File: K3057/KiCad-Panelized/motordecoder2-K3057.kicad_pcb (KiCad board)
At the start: 2 copper layers, 85 x 94 mm, 522 parts, among them J11 PAD, J12 PAD, J14 PAD, J16 PAD, J18 PAD, J19 PAD, P10 PAD, P11 PAD, P21 PAD, P22 PAD, P23 PAD, P24 PAD, P25 PAD, P26 PAD, P27 PAD, P28 PAD, P29 PAD, P31 PAD, P7 PAD, P8 PAD, P9 PROG, Q1 DMG6601LVT, Q11 SSM6N7002BFE, Q12 SSM6N7002BFE, Q13 SSM6N7002BFE, Q14 SSM6N7002BFE, Q15 SSM3K7002BFU, Q2 DMG6601LVT, Q21 PMBT3906VS, Q22 SSM6N7002BFE, Q3 PMBT3904VS, Q5 2SC4116, Q6 PMBT3906VS, Q8 PMBT3904VS, U2 ATtiny1606-M

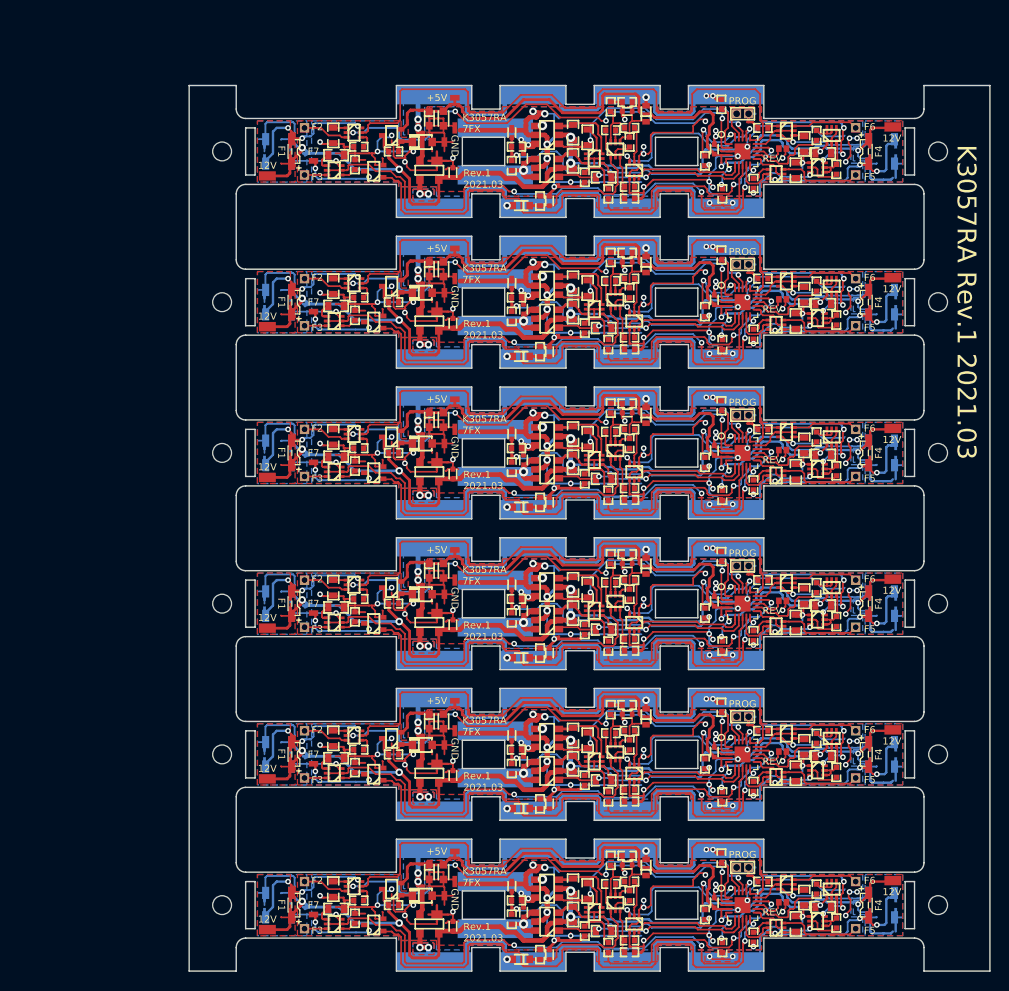
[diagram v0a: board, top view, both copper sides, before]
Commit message: 回路の問題点を修正 (K3066: Rev3 / それ以外: Rev2)
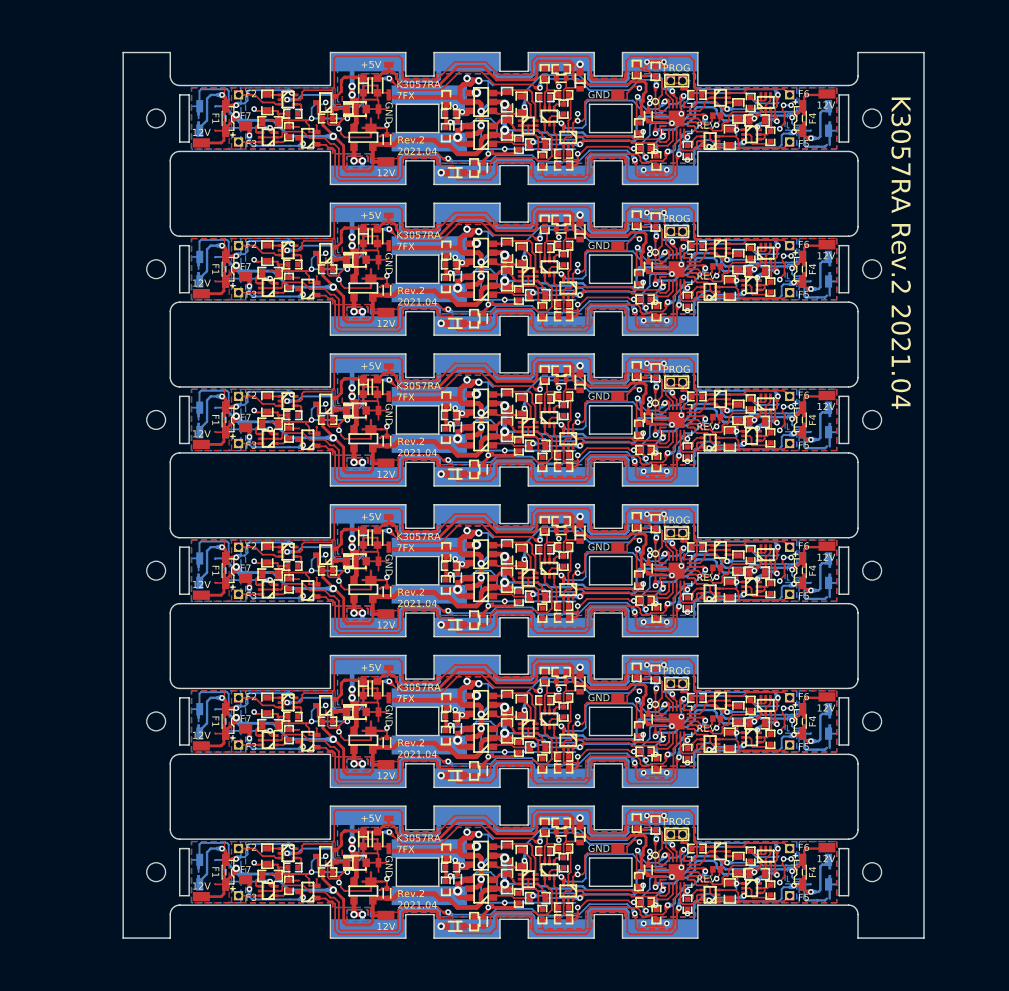
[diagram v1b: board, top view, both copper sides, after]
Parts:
- removed the C1 at (136.0, 126.2)
- removed the C1 at (136.0, 110.2)
- removed the C1 at (136.0, 94.2)
- removed the C1 at (136.0, 78.2)
- removed the C1 at (136.0, 62.2)
- removed the C11 at (154.5, 119.8)
- removed the C11 at (154.5, 103.8)
- removed the C11 at (154.5, 87.8)
- removed the C11 at (154.5, 71.8)
- removed the C11 at (154.5, 55.8)
- removed the C12 at (146.2, 129.2)
- removed the C12 at (146.2, 113.2)
- removed the C12 at (146.2, 97.2)
- removed the C12 at (146.2, 81.2)
- removed the C12 at (146.2, 65.2)
- removed the C3 at (135.0, 120.5)
- removed the C3 at (135.0, 104.5)
- removed the C3 at (135.0, 88.5)
- removed the C3 at (135.0, 72.5)
- removed the C3 at (135.0, 56.5)
- removed the C4 at (133.5, 120.5)
- removed the C4 at (133.5, 104.5)
- removed the C4 at (133.5, 88.5)
- removed the C4 at (133.5, 72.5)
- removed the C4 at (133.5, 56.5)
- removed the C5 at (163.8, 123.8)
- removed the C5 at (163.8, 107.8)
- removed the C5 at (163.8, 91.8)
- removed the C5 at (163.8, 75.8)
- removed the C5 at (163.8, 59.8)
- removed C6 (x6): 104, footprint:C_1005_v2
- removed the C7 at (143.5, 124.8)
- removed the C7 at (143.5, 108.8)
- removed the C7 at (143.5, 92.8)
- removed the C7 at (143.5, 76.8)
- removed the C7 at (143.5, 60.8)
- removed the D1 at (133.5, 126.0)
- removed the D1 at (133.5, 110.0)
- removed the D1 at (133.5, 94.0)
- removed the D1 at (133.5, 78.0)
- removed the D1 at (133.5, 62.0)
- removed the D11 at (118.5, 124.0)
- removed the D11 at (118.5, 108.0)
- removed the D11 at (118.5, 92.0)
- removed the D11 at (118.5, 76.0)
- removed the D11 at (118.5, 60.0)
- removed the D12 at (180.5, 124.0)
- removed the D12 at (180.5, 108.0)
- removed the D12 at (180.5, 92.0)
- removed the D12 at (180.5, 76.0)
- removed the D12 at (180.5, 60.0)
- removed the D13 at (115.8, 124.0)
- removed the D13 at (115.8, 108.0)
- removed the D13 at (115.8, 92.0)
- removed the D13 at (115.8, 76.0)
- removed the D13 at (115.8, 60.0)
- removed the D14 at (183.2, 124.0)
- removed the D14 at (183.2, 108.0)
- removed the D14 at (183.2, 92.0)
- removed the D14 at (183.2, 76.0)
- removed the D14 at (183.2, 60.0)
- removed the D15 at (180.5, 124.0)
- removed the D15 at (180.5, 108.0)
- removed the D15 at (180.5, 92.0)
- removed the D15 at (180.5, 76.0)
- removed the D15 at (180.5, 60.0)
- removed the D16 at (118.5, 124.0)
- removed the D16 at (118.5, 108.0)
- removed the D16 at (118.5, 92.0)
- removed the D16 at (118.5, 76.0)
- removed the D16 at (118.5, 60.0)
- removed the D21 at (156.5, 120.0)
- removed the D21 at (156.5, 104.0)
- removed the D21 at (156.5, 88.0)
- removed the D21 at (156.5, 72.0)
- removed the D21 at (156.5, 56.0)
- removed the D22 at (143.2, 129.8)
- removed the D22 at (143.2, 113.8)
- removed the D22 at (143.2, 97.8)
- removed the D22 at (143.2, 81.8)
- removed the D22 at (143.2, 65.8)
- removed the D3 at (132.8, 123.0)
- removed the D3 at (132.8, 107.0)
- removed the D3 at (132.8, 91.0)
- removed the D3 at (132.8, 75.0)
- removed the D3 at (132.8, 59.0)
- removed the J11 at (182.7, 121.4)
- removed the J11 at (182.7, 105.4)
- removed the J11 at (182.7, 89.4)
- removed the J11 at (182.7, 73.4)
- removed the J11 at (182.7, 57.4)
- removed the J12 at (178.8, 126.5)
- removed the J12 at (178.8, 110.5)
- removed the J12 at (178.8, 94.5)
- removed the J12 at (178.8, 78.5)
- removed the J12 at (178.8, 62.5)
- removed the J14 at (120.2, 126.5)
- removed the J14 at (120.2, 110.5)
- removed the J14 at (120.2, 94.5)
- removed the J14 at (120.2, 78.5)
- removed the J14 at (120.2, 62.5)
- removed the J16 at (178.8, 121.5)
- removed the J16 at (178.8, 105.5)
- removed the J16 at (178.8, 89.5)
- removed the J16 at (178.8, 73.5)
- removed the J16 at (178.8, 57.5)
- removed the J18 at (120.2, 121.5)
- removed the J18 at (120.2, 105.5)
- removed the J18 at (120.2, 89.5)
- removed the J18 at (120.2, 73.5)
- removed the J18 at (120.2, 57.5)
- removed the J19 at (121.2, 125.0)
- removed the J19 at (121.2, 109.0)
- removed the J19 at (121.2, 93.0)
- removed the J19 at (121.2, 77.0)
- removed the J19 at (121.2, 61.0)
- removed the J19 at (121.2, 45.0)
- removed the JP1 at (171.0, 123.7)
- removed the JP1 at (171.0, 107.7)
- removed the JP1 at (171.0, 91.7)
- removed the JP1 at (171.0, 75.7)
- removed the JP1 at (171.0, 59.7)
- removed the P10 at (136.2, 118.3)
- removed the P10 at (136.2, 102.3)
- removed the P10 at (136.2, 86.3)
- removed the P10 at (136.2, 70.3)
- removed the P10 at (136.2, 54.3)
- removed the P11 at (136.2, 121.5)
- removed the P11 at (136.2, 105.5)
- removed the P11 at (136.2, 89.5)
- removed the P11 at (136.2, 73.5)
- removed the P11 at (136.2, 57.5)
- removed the P21 at (134.0, 118.0)
- removed the P21 at (134.0, 102.0)
- removed the P21 at (134.0, 86.0)
- removed the P21 at (134.0, 70.0)
- removed the P21 at (134.0, 54.0)
- removed the P22 at (144.5, 118.0)
- removed the P22 at (144.5, 102.0)
- removed the P22 at (144.5, 86.0)
- removed the P22 at (144.5, 70.0)
- removed the P22 at (144.5, 54.0)
- removed the P23 at (154.5, 118.0)
- removed the P23 at (154.5, 102.0)
- removed the P23 at (154.5, 86.0)
- removed the P23 at (154.5, 70.0)
- removed the P23 at (154.5, 54.0)
- removed the P24 at (165.0, 118.0)
- removed the P24 at (165.0, 102.0)
- removed the P24 at (165.0, 86.0)
- removed the P24 at (165.0, 70.0)
- removed the P24 at (165.0, 54.0)
- removed the P25 at (134.0, 130.0)
- removed the P25 at (134.0, 114.0)
- removed the P25 at (134.0, 98.0)
- removed the P25 at (134.0, 82.0)
- removed the P25 at (134.0, 66.0)
- removed the P26 at (144.5, 130.0)
- removed the P26 at (144.5, 114.0)
- removed the P26 at (144.5, 98.0)
- removed the P26 at (144.5, 82.0)
- removed the P26 at (144.5, 66.0)
- removed the P27 at (154.5, 130.0)
- removed the P27 at (154.5, 114.0)
- removed the P27 at (154.5, 98.0)
- removed the P27 at (154.5, 82.0)
- removed the P27 at (154.5, 66.0)
- removed the P28 at (165.0, 130.0)
- removed the P28 at (165.0, 114.0)
- removed the P28 at (165.0, 98.0)
- removed the P28 at (165.0, 82.0)
- removed the P28 at (165.0, 66.0)
- removed the P29 at (140.5, 121.5)
- removed the P29 at (140.5, 105.5)
- removed the P29 at (140.5, 89.5)
- removed the P29 at (140.5, 73.5)
- removed the P29 at (140.5, 57.5)
- removed the P31 at (140.5, 126.5)
- removed the P31 at (140.5, 110.5)
- removed the P31 at (140.5, 94.5)
- removed the P31 at (140.5, 78.5)
- removed the P31 at (140.5, 62.5)
- removed the P7 at (116.3, 126.6)
- removed the P7 at (116.3, 110.6)
- removed the P7 at (116.3, 94.6)
- removed the P7 at (116.3, 78.6)
- removed the P7 at (116.3, 62.6)
- removed the P8 at (135.1, 123.0)
- removed the P8 at (135.1, 107.0)
- removed the P8 at (135.1, 91.0)
- removed the P8 at (135.1, 75.0)
- removed the P8 at (135.1, 59.0)
- removed the P9 at (166.8, 120.0)
- removed the P9 at (166.8, 104.0)
- removed the P9 at (166.8, 88.0)
- removed the P9 at (166.8, 72.0)
- removed the P9 at (166.8, 56.0)
- removed the Q1 at (146.0, 122.2)
- removed the Q1 at (146.0, 106.2)
- removed the Q1 at (146.0, 90.2)
- removed the Q1 at (146.0, 74.2)
- removed the Q1 at (146.0, 58.2)
- removed the Q11 at (125.5, 122.0)
- removed the Q11 at (125.5, 106.0)
- removed the Q11 at (125.5, 90.0)
- removed the Q11 at (125.5, 74.0)
- removed the Q11 at (125.5, 58.0)
- removed the Q12 at (170.3, 126.4)
- removed the Q12 at (170.3, 110.4)
- removed the Q12 at (170.3, 94.4)
- removed the Q12 at (170.3, 78.4)
- removed the Q12 at (170.3, 62.4)
- removed the Q13 at (123.4, 126.0)
- removed the Q13 at (123.4, 110.0)
- removed the Q13 at (123.4, 94.0)
- removed the Q13 at (123.4, 78.0)
- removed the Q13 at (123.4, 62.0)
- removed the Q14 at (171.4, 121.8)
- removed the Q14 at (171.4, 105.8)
- removed the Q14 at (171.4, 89.8)
- removed the Q14 at (171.4, 73.8)
- removed the Q14 at (171.4, 57.8)
- removed the Q15 at (127.6, 126.1)
- removed the Q15 at (127.6, 110.1)
- removed the Q15 at (127.6, 94.1)
- removed the Q15 at (127.6, 78.1)
- removed the Q15 at (127.6, 62.1)
- removed the Q2 at (146.0, 125.8)
- removed the Q2 at (146.0, 109.8)
- removed the Q2 at (146.0, 93.8)
- removed the Q2 at (146.0, 77.8)
- removed the Q2 at (146.0, 61.8)
- removed the Q21 at (153.2, 123.8)
- removed the Q21 at (153.2, 107.8)
- removed the Q21 at (153.2, 91.8)
- removed the Q21 at (153.2, 75.8)
- removed the Q21 at (153.2, 59.8)
- removed the Q22 at (155.2, 126.0)
- removed the Q22 at (155.2, 110.0)
- removed the Q22 at (155.2, 94.0)
- removed the Q22 at (155.2, 78.0)
- removed the Q22 at (155.2, 62.0)
- removed the Q3 at (151.0, 124.8)
- removed the Q3 at (151.0, 108.8)
- removed the Q3 at (151.0, 92.8)
- removed the Q3 at (151.0, 76.8)
- removed the Q3 at (151.0, 60.8)
- removed the Q5 at (129.5, 122.3)
- removed the Q5 at (129.5, 106.3)
- removed the Q5 at (129.5, 90.3)
- removed the Q5 at (129.5, 74.3)
- removed the Q5 at (129.5, 58.3)
- removed the Q6 at (176.2, 122.3)
- removed the Q6 at (176.2, 106.3)
- removed the Q6 at (176.2, 90.3)
- removed the Q6 at (176.2, 74.3)
- removed the Q6 at (176.2, 58.3)
- removed the Q8 at (174.7, 125.7)
- removed the Q8 at (174.7, 109.7)
- removed the Q8 at (174.7, 93.7)
- removed the Q8 at (174.7, 77.7)
- removed the Q8 at (174.7, 61.7)
- removed the R1 at (164.5, 119.0)
- removed the R1 at (164.5, 103.0)
- removed the R1 at (164.5, 87.0)
- removed the R1 at (164.5, 71.0)
- removed the R1 at (164.5, 55.0)
- removed the R10 at (142.2, 125.5)
- removed the R10 at (142.2, 109.5)
- removed the R10 at (142.2, 93.5)
- removed the R10 at (142.2, 77.5)
- removed the R10 at (142.2, 61.5)
- removed the R11 at (162.8, 125.0)
- removed the R11 at (162.8, 109.0)
- removed the R11 at (162.8, 93.0)
- removed the R11 at (162.8, 77.0)
- removed the R11 at (162.8, 61.0)
- removed the R12 at (129.7, 124.0)
- removed the R12 at (129.7, 108.0)
- removed the R12 at (129.7, 92.0)
- removed the R12 at (129.7, 76.0)
- removed the R12 at (129.7, 60.0)
- removed the R13 at (174.6, 122.3)
- removed the R13 at (174.6, 106.3)
- removed the R13 at (174.6, 90.3)
- removed the R13 at (174.6, 74.3)
- removed the R13 at (174.6, 58.3)
- removed the R14 at (175.3, 124.2)
- removed the R14 at (175.3, 108.2)
- removed the R14 at (175.3, 92.2)
- removed the R14 at (175.3, 76.2)
- removed the R14 at (175.3, 60.2)
- removed the R15 at (176.7, 125.9)
- removed the R15 at (176.7, 109.9)
- removed the R15 at (176.7, 93.9)
- removed the R15 at (176.7, 77.9)
- removed the R15 at (176.7, 61.9)
- removed the R2 at (164.6, 128.5)
- removed the R2 at (164.6, 112.5)
- removed the R2 at (164.6, 96.5)
- removed the R2 at (164.6, 80.5)
- removed the R2 at (164.6, 64.5)
- removed the R21 at (123.3, 122.3)
- removed the R21 at (123.3, 106.3)
- removed the R21 at (123.3, 90.3)
- removed the R21 at (123.3, 74.3)
- removed the R21 at (123.3, 58.3)
- removed the R22 at (172.4, 126.0)
- removed the R22 at (172.4, 110.0)
- removed the R22 at (172.4, 94.0)
- removed the R22 at (172.4, 78.0)
- removed the R22 at (172.4, 62.0)
- removed the R23 at (167.9, 127.4)
- removed the R23 at (167.9, 111.4)
- removed the R23 at (167.9, 95.4)
- removed the R23 at (167.9, 79.4)
- removed the R23 at (167.9, 63.4)
- removed the R24 at (125.6, 125.4)
- removed the R24 at (125.6, 109.4)
- removed the R24 at (125.6, 93.4)
- removed the R24 at (125.6, 77.4)
- removed the R24 at (125.6, 61.4)
- removed the R25 at (168.9, 121.5)
- removed the R25 at (168.9, 105.5)
- removed the R25 at (168.9, 89.5)
- removed the R25 at (168.9, 73.5)
- removed the R25 at (168.9, 57.5)
- removed the R26 at (126.0, 123.5)
- removed the R26 at (126.0, 107.5)
- removed the R26 at (126.0, 91.5)
- removed the R26 at (126.0, 75.5)
- removed the R26 at (126.0, 59.5)
- removed the R27 at (123.6, 124.4)
- removed the R27 at (123.6, 108.4)
- removed the R27 at (123.6, 92.4)
- removed the R27 at (123.6, 76.4)
- removed the R27 at (123.6, 60.4)
- removed the R28 at (173.3, 123.2)
- removed the R28 at (173.3, 107.2)
- removed the R28 at (173.3, 91.2)
- removed the R28 at (173.3, 75.2)
- removed the R28 at (173.3, 59.2)
- removed the R3 at (148.8, 122.0)
- removed the R3 at (148.8, 106.0)
- removed the R3 at (148.8, 90.0)
- removed the R3 at (148.8, 74.0)
- removed the R3 at (148.8, 58.0)
- removed the R31 at (154.8, 123.0)
- removed the R31 at (154.8, 107.0)
- removed the R31 at (154.8, 91.0)
- removed the R31 at (154.8, 75.0)
- removed the R31 at (154.8, 59.0)
- removed the R32 at (154.5, 118.8)
- removed the R32 at (154.5, 102.8)
- removed the R32 at (154.5, 86.8)
- removed the R32 at (154.5, 70.8)
- removed the R32 at (154.5, 54.8)
- removed the R33 at (152.8, 119.2)
- removed the R33 at (152.8, 103.2)
- removed the R33 at (152.8, 87.2)
- removed the R33 at (152.8, 71.2)
- removed the R33 at (152.8, 55.2)
- removed the R34 at (154.8, 121.5)
- removed the R34 at (154.8, 105.5)
- removed the R34 at (154.8, 89.5)
- removed the R34 at (154.8, 73.5)
- removed the R34 at (154.8, 57.5)
- removed the R35 at (152.8, 121.8)
- removed the R35 at (152.8, 105.8)
- removed the R35 at (152.8, 89.8)
- removed the R35 at (152.8, 73.8)
- removed the R35 at (152.8, 57.8)
- removed the R36 at (145.2, 129.2)
- removed the R36 at (145.2, 113.2)
- removed the R36 at (145.2, 97.2)
- removed the R36 at (145.2, 81.2)
- removed the R36 at (145.2, 65.2)
- removed the R37 at (154.8, 129.0)
- removed the R37 at (154.8, 113.0)
- removed the R37 at (154.8, 97.0)
- removed the R37 at (154.8, 81.0)
- removed the R37 at (154.8, 65.0)
- removed the R38 at (154.8, 127.8)
- removed the R38 at (154.8, 111.8)
- removed the R38 at (154.8, 95.8)
- removed the R38 at (154.8, 79.8)
- removed the R38 at (154.8, 63.8)
- removed the R4 at (148.8, 125.0)
- removed the R4 at (148.8, 109.0)
- removed the R4 at (148.8, 93.0)
- removed the R4 at (148.8, 77.0)
- removed the R4 at (148.8, 61.0)
- removed the R5 at (150.3, 122.5)
- removed the R5 at (150.3, 106.5)
- removed the R5 at (150.3, 90.5)
- removed the R5 at (150.3, 74.5)
- removed the R5 at (150.3, 58.5)
- removed the R6 at (152.0, 126.8)
- removed the R6 at (152.0, 110.8)
- removed the R6 at (152.0, 94.8)
- removed the R6 at (152.0, 78.8)
- removed the R6 at (152.0, 62.8)
- removed the R7 at (152.5, 128.5)
- removed the R7 at (152.5, 112.5)
- removed the R7 at (152.5, 96.5)
- removed the R7 at (152.5, 80.5)
- removed the R7 at (152.5, 64.5)
- removed the R8 at (150.0, 126.8)
- removed the R8 at (150.0, 110.8)
- removed the R8 at (150.0, 94.8)
- removed the R8 at (150.0, 78.8)
- removed the R8 at (150.0, 62.8)
- removed the R9 at (142.8, 123.5)
- removed the R9 at (142.8, 107.5)
- removed the R9 at (142.8, 91.5)
- removed the R9 at (142.8, 75.5)
- removed the R9 at (142.8, 59.5)
- removed the REF** at (187.5, 60.0)
- removed the REF** at (111.5, 60.0)
- removed the REF** at (187.5, 44.0)
- removed the REF** at (111.5, 44.0)
- removed the REF** at (187.5, 76.0)
- removed the REF** at (187.5, 92.0)
- removed the REF** at (187.5, 108.0)
- removed the REF** at (187.5, 124.0)
- removed the REF** at (111.5, 124.0)
- removed the REF** at (111.5, 108.0)
- removed the REF** at (111.5, 92.0)
- removed the REF** at (111.5, 76.0)
- removed the U2 at (166.8, 124.0)
- removed the U2 at (166.8, 108.0)
- removed the U2 at (166.8, 92.0)
- removed the U2 at (166.8, 76.0)
- removed the U2 at (166.8, 60.0)
- added C1: 104, footprint:C_1005_v2, F.Cu at (129.0, 122.8)
- added C1: 104, footprint:C_1005_v2, F.Cu at (129.0, 106.8)
- added C1: 104, footprint:C_1005_v2, F.Cu at (129.0, 90.8)
- added C1: 104, footprint:C_1005_v2, F.Cu at (129.0, 74.8)
- added C1: 104, footprint:C_1005_v2, F.Cu at (129.0, 58.8)
- added C11: 105, footprint:C_1005_v2, F.Cu at (147.5, 116.2)
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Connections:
- net Func8 renamed DIR_JP
- Q11 pad 5: Func6 -> Func2
- Q12 pad 2: Func2 -> Func4
- Q12 pad 5: Func3 -> Func5
- Q13 pad 2: Func4 -> Func3
- Q13 pad 5: Func4 -> Func3
- Q14 pad 2: Func5 -> Func6
- Q14 pad 5: Func5 -> Func6
- U2 pad 11: Func2 -> Func4
- U2 pad 15: Func5 -> Func6
- U2 pad 16: Func6 -> Func2
- U2 pad 8: Func4 -> Func3
- U2 pad 9: Func3 -> Func5
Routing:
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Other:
- rule pad_to_mask_clearance: 0 -> 0.05
- board text added: "K3057RA Rev.2 2021.04"
- board text added: "Rev.2 2021.04"
- board text removed: "K3057RA Rev.1 2021.03"
- board text removed: "Rev.1 2021.03"

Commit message: 基板上のF表記をP表記に変更
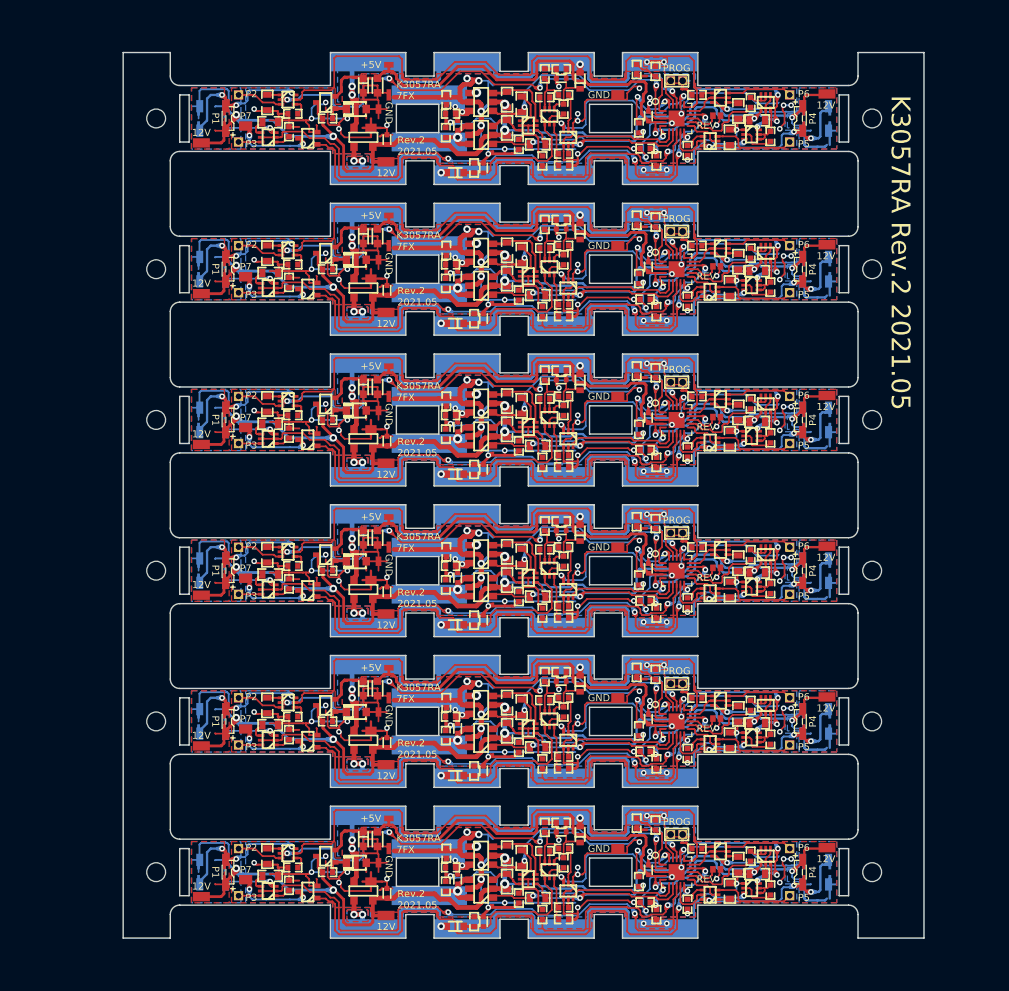
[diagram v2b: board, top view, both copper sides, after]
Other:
- board text added: "K3057RA Rev.2 2021.05"
- board text added: "P1"
- board text added: "P2"
- board text added: "P3"
- board text added: "P4"
- board text added: "P5"
- board text added: "P6"
- board text added: "P7"
- board text added: "Rev.2 2021.05"
- board text removed: "F1"
- board text removed: "F2"
- board text removed: "F3"
- board text removed: "F4"
- board text removed: "F5"
- board text removed: "F6"
- board text removed: "F7"
- board text removed: "K3057RA Rev.2 2021.04"
- board text removed: "Rev.2 2021.04"

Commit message: (K3057RA) 表面のLEDパッドを増設
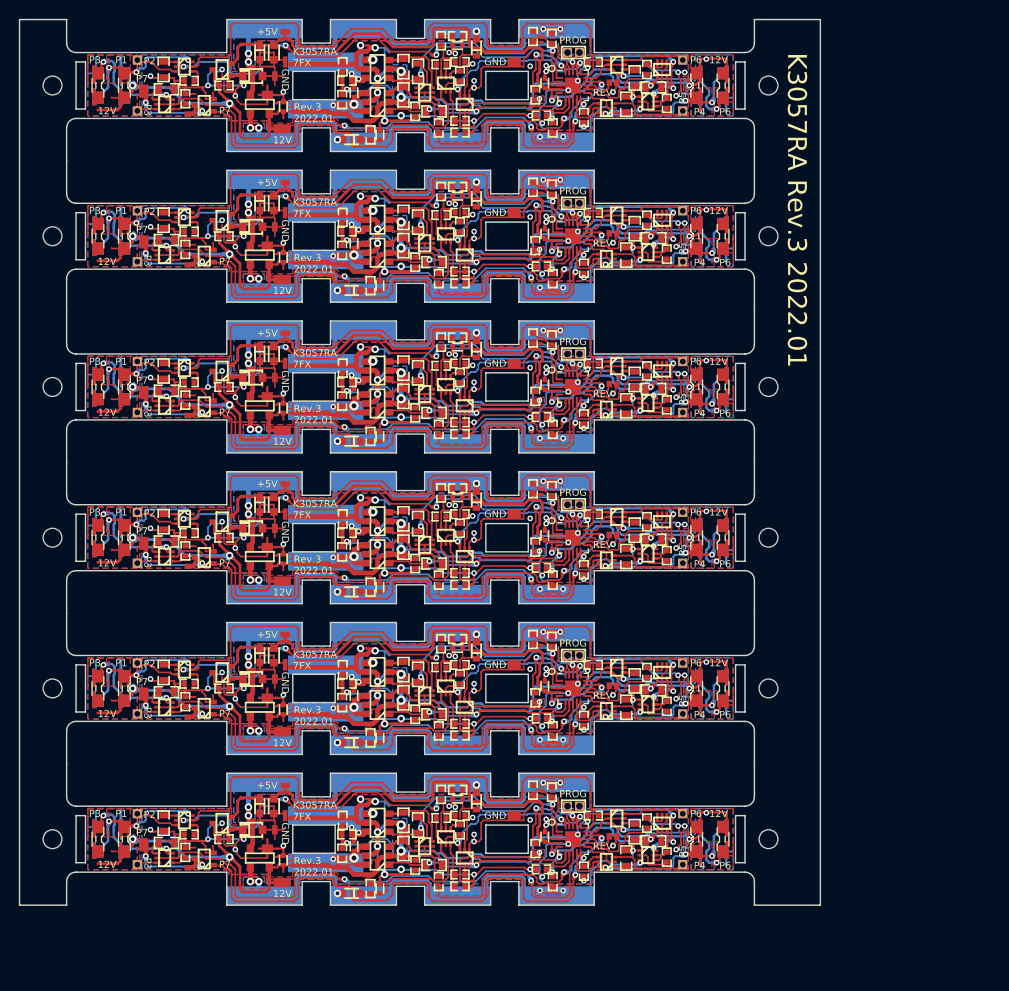
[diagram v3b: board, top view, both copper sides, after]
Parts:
- removed the C1 at (129.0, 122.8)
- removed the C1 at (129.0, 106.8)
- removed the C1 at (129.0, 90.8)
- removed the C1 at (129.0, 74.8)
- removed the C1 at (129.0, 58.8)
- removed the C11 at (147.5, 116.2)
- removed the C11 at (147.5, 100.2)
- removed the C11 at (147.5, 84.2)
- removed the C11 at (147.5, 68.2)
- removed the C11 at (147.5, 52.2)
- removed the C12 at (139.2, 125.8)
- removed the C12 at (139.2, 109.8)
- removed the C12 at (139.2, 93.8)
- removed the C12 at (139.2, 77.8)
- removed the C12 at (139.2, 61.8)
- removed the C3 at (128.0, 117.0)
- removed the C3 at (128.0, 101.0)
- removed the C3 at (128.0, 85.0)
- removed the C3 at (128.0, 69.0)
- removed the C3 at (128.0, 53.0)
- removed the C4 at (126.5, 117.0)
- removed the C4 at (126.5, 101.0)
- removed the C4 at (126.5, 85.0)
- removed the C4 at (126.5, 69.0)
- removed the C4 at (126.5, 53.0)
- removed the C5 at (156.8, 120.2)
- removed the C5 at (156.8, 104.2)
- removed the C5 at (156.8, 88.2)
- removed the C5 at (156.8, 72.2)
- removed the C5 at (156.8, 56.2)
- removed the C7 at (136.5, 121.2)
- removed the C7 at (136.5, 105.2)
- removed the C7 at (136.5, 89.2)
- removed the C7 at (136.5, 73.2)
- removed the C7 at (136.5, 57.2)
- removed the D1 at (126.5, 122.5)
- removed the D1 at (126.5, 106.5)
- removed the D1 at (126.5, 90.5)
- removed the D1 at (126.5, 74.5)
- removed the D1 at (126.5, 58.5)
- removed the D11 at (111.5, 120.5)
- removed the D11 at (111.5, 104.5)
- removed the D11 at (111.5, 88.5)
- removed the D11 at (111.5, 72.5)
- removed the D11 at (111.5, 56.5)
- removed the D11 at (111.5, 40.5)
- removed the D12 at (173.5, 120.5)
- removed the D12 at (173.5, 104.5)
- removed the D12 at (173.5, 88.5)
- removed the D12 at (173.5, 72.5)
- removed the D12 at (173.5, 56.5)
- removed the D12 at (173.5, 40.5)
- removed the D13 at (108.8, 120.5)
- removed the D13 at (108.8, 104.5)
- removed the D13 at (108.8, 88.5)
- removed the D13 at (108.8, 72.5)
- removed the D13 at (108.8, 56.5)
- removed the D13 at (108.8, 40.5)
- removed the D14 at (176.2, 120.5)
- removed the D14 at (176.2, 104.5)
- removed the D14 at (176.2, 88.5)
- removed the D14 at (176.2, 72.5)
- removed the D14 at (176.2, 56.5)
- removed the D14 at (176.2, 40.5)
- removed the D15 at (173.5, 120.5)
- removed the D15 at (173.5, 104.5)
- removed the D15 at (173.5, 88.5)
- removed the D15 at (173.5, 72.5)
- removed the D15 at (173.5, 56.5)
- removed the D15 at (173.5, 40.5)
- removed the D16 at (111.5, 120.5)
- removed the D16 at (111.5, 104.5)
- removed the D16 at (111.5, 88.5)
- removed the D16 at (111.5, 72.5)
- removed the D16 at (111.5, 56.5)
- removed the D16 at (111.5, 40.5)
- removed the D21 at (149.5, 116.5)
- removed the D21 at (149.5, 100.5)
- removed the D21 at (149.5, 84.5)
- removed the D21 at (149.5, 68.5)
- removed the D21 at (149.5, 52.5)
- removed the D22 at (136.2, 126.2)
- removed the D22 at (136.2, 110.2)
- removed the D22 at (136.2, 94.2)
- removed the D22 at (136.2, 78.2)
- removed the D22 at (136.2, 62.2)
- removed the D3 at (125.8, 119.5)
- removed the D3 at (125.8, 103.5)
- removed the D3 at (125.8, 87.5)
- removed the D3 at (125.8, 71.5)
- removed the D3 at (125.8, 55.5)
- removed J11 (x6), J13 (x6): PAD, footprint:PAD_1.0x1.8_SMD
- removed the J12 at (171.8, 123.0)
- removed the J12 at (171.8, 107.0)
- removed the J12 at (171.8, 91.0)
- removed the J12 at (171.8, 75.0)
- removed the J12 at (171.8, 59.0)
- removed the J14 at (113.2, 123.0)
- removed the J14 at (113.2, 107.0)
- removed the J14 at (113.2, 91.0)
- removed the J14 at (113.2, 75.0)
- removed the J14 at (113.2, 59.0)
- removed the J16 at (171.8, 118.0)
- removed the J16 at (171.8, 102.0)
- removed the J16 at (171.8, 86.0)
- removed the J16 at (171.8, 70.0)
- removed the J16 at (171.8, 54.0)
- removed the J18 at (113.2, 118.0)
- removed the J18 at (113.2, 102.0)
- removed the J18 at (113.2, 86.0)
- removed the J18 at (113.2, 70.0)
- removed the J18 at (113.2, 54.0)
- removed the J19 at (114.0, 121.3)
- removed the J19 at (114.0, 105.3)
- removed the J19 at (114.0, 89.3)
- removed the J19 at (114.0, 73.3)
- removed the J19 at (114.0, 57.3)
- removed the JP1 at (164.0, 120.2)
- removed the JP1 at (164.0, 104.2)
- removed the JP1 at (164.0, 88.2)
- removed the JP1 at (164.0, 72.2)
- removed the JP1 at (164.0, 56.2)
- removed the P10 at (129.2, 114.8)
- removed the P10 at (129.2, 98.8)
- removed the P10 at (129.2, 82.8)
- removed the P10 at (129.2, 66.8)
- removed the P10 at (129.2, 50.8)
- removed the P11 at (129.2, 118.0)
- removed the P11 at (129.2, 102.0)
- removed the P11 at (129.2, 86.0)
- removed the P11 at (129.2, 70.0)
- removed the P11 at (129.2, 54.0)
- removed the P12 at (153.5, 118.0)
- removed the P12 at (153.5, 102.0)
- removed the P12 at (153.5, 86.0)
- removed the P12 at (153.5, 70.0)
- removed the P12 at (153.5, 54.0)
- removed the P21 at (127.0, 114.5)
- removed the P21 at (127.0, 98.5)
- removed the P21 at (127.0, 82.5)
- removed the P21 at (127.0, 66.5)
- removed the P21 at (127.0, 50.5)
- removed the P22 at (137.5, 114.5)
- removed the P22 at (137.5, 98.5)
- removed the P22 at (137.5, 82.5)
- removed the P22 at (137.5, 66.5)
- removed the P22 at (137.5, 50.5)
- removed the P23 at (147.5, 114.5)
- removed the P23 at (147.5, 98.5)
- removed the P23 at (147.5, 82.5)
- removed the P23 at (147.5, 66.5)
- removed the P23 at (147.5, 50.5)
- removed the P24 at (158.0, 114.5)
- removed the P24 at (158.0, 98.5)
- removed the P24 at (158.0, 82.5)
- removed the P24 at (158.0, 66.5)
- removed the P24 at (158.0, 50.5)
- removed the P25 at (127.0, 126.5)
- removed the P25 at (127.0, 110.5)
- removed the P25 at (127.0, 94.5)
- removed the P25 at (127.0, 78.5)
- removed the P25 at (127.0, 62.5)
- removed the P26 at (137.5, 126.5)
- removed the P26 at (137.5, 110.5)
- removed the P26 at (137.5, 94.5)
- removed the P26 at (137.5, 78.5)
- removed the P26 at (137.5, 62.5)
- removed the P27 at (147.5, 126.5)
- removed the P27 at (147.5, 110.5)
- removed the P27 at (147.5, 94.5)
- removed the P27 at (147.5, 78.5)
- removed the P27 at (147.5, 62.5)
- removed the P28 at (158.0, 126.5)
- removed the P28 at (158.0, 110.5)
- removed the P28 at (158.0, 94.5)
- removed the P28 at (158.0, 78.5)
- removed the P28 at (158.0, 62.5)
- removed the P29 at (133.5, 118.0)
- removed the P29 at (133.5, 102.0)
- removed the P29 at (133.5, 86.0)
- removed the P29 at (133.5, 70.0)
- removed the P29 at (133.5, 54.0)
- removed the P31 at (133.5, 123.0)
- removed the P31 at (133.5, 107.0)
- removed the P31 at (133.5, 91.0)
- removed the P31 at (133.5, 75.0)
- removed the P31 at (133.5, 59.0)
- removed the P7 at (109.3, 123.1)
- removed the P7 at (109.3, 107.1)
- removed the P7 at (109.3, 91.1)
- removed the P7 at (109.3, 75.1)
- removed the P7 at (109.3, 59.1)
- removed the P8 at (128.1, 119.5)
- removed the P8 at (128.1, 103.5)
- removed the P8 at (128.1, 87.5)
- removed the P8 at (128.1, 71.5)
- removed the P8 at (128.1, 55.5)
- removed the P9 at (159.8, 116.5)
- removed the P9 at (159.8, 100.5)
- removed the P9 at (159.8, 84.5)
- removed the P9 at (159.8, 68.5)
- removed the P9 at (159.8, 52.5)
- removed the Q1 at (139.0, 118.8)
- removed the Q1 at (139.0, 102.8)
- removed the Q1 at (139.0, 86.8)
- removed the Q1 at (139.0, 70.8)
- removed the Q1 at (139.0, 54.8)
- removed the Q11 at (118.5, 118.5)
- removed the Q11 at (118.5, 102.5)
- removed the Q11 at (118.5, 86.5)
- removed the Q11 at (118.5, 70.5)
- removed the Q11 at (118.5, 54.5)
- removed the Q12 at (163.3, 122.9)
- removed the Q12 at (163.3, 106.9)
- removed the Q12 at (163.3, 90.9)
- removed the Q12 at (163.3, 74.9)
- removed the Q12 at (163.3, 58.9)
- removed the Q13 at (116.4, 122.5)
- removed the Q13 at (116.4, 106.5)
- removed the Q13 at (116.4, 90.5)
- removed the Q13 at (116.4, 74.5)
- removed the Q13 at (116.4, 58.5)
- removed the Q14 at (164.4, 118.3)
- removed the Q14 at (164.4, 102.3)
- removed the Q14 at (164.4, 86.3)
- removed the Q14 at (164.4, 70.3)
- removed the Q14 at (164.4, 54.3)
- removed the Q15 at (120.6, 122.6)
- removed the Q15 at (120.6, 106.6)
- removed the Q15 at (120.6, 90.6)
- removed the Q15 at (120.6, 74.6)
- removed the Q15 at (120.6, 58.6)
- removed the Q2 at (139.0, 122.2)
- removed the Q2 at (139.0, 106.2)
- removed the Q2 at (139.0, 90.2)
- removed the Q2 at (139.0, 74.2)
- removed the Q2 at (139.0, 58.2)
- removed the Q21 at (146.2, 120.2)
- removed the Q21 at (146.2, 104.2)
- removed the Q21 at (146.2, 88.2)
- removed the Q21 at (146.2, 72.2)
- removed the Q21 at (146.2, 56.2)
- removed the Q22 at (148.2, 122.5)
- removed the Q22 at (148.2, 106.5)
- removed the Q22 at (148.2, 90.5)
- removed the Q22 at (148.2, 74.5)
- removed the Q22 at (148.2, 58.5)
- removed the Q3 at (144.0, 121.2)
- removed the Q3 at (144.0, 105.2)
- removed the Q3 at (144.0, 89.2)
- removed the Q3 at (144.0, 73.2)
- removed the Q3 at (144.0, 57.2)
- removed the Q5 at (122.5, 118.8)
- removed the Q5 at (122.5, 102.8)
- removed the Q5 at (122.5, 86.8)
- removed the Q5 at (122.5, 70.8)
- removed the Q5 at (122.5, 54.8)
- removed the Q6 at (169.2, 118.8)
- removed the Q6 at (169.2, 102.8)
- removed the Q6 at (169.2, 86.8)
- removed the Q6 at (169.2, 70.8)
- removed the Q6 at (169.2, 54.8)
- removed the Q8 at (167.7, 122.2)
- removed the Q8 at (167.7, 106.2)
- removed the Q8 at (167.7, 90.2)
- removed the Q8 at (167.7, 74.2)
- removed the Q8 at (167.7, 58.2)
- removed the R1 at (157.5, 115.5)
- removed the R1 at (157.5, 99.5)
- removed the R1 at (157.5, 83.5)
- removed the R1 at (157.5, 67.5)
- removed the R1 at (157.5, 51.5)
- removed the R10 at (135.2, 122.0)
- removed the R10 at (135.2, 106.0)
- removed the R10 at (135.2, 90.0)
- removed the R10 at (135.2, 74.0)
- removed the R10 at (135.2, 58.0)
- removed the R11 at (155.8, 121.5)
- removed the R11 at (155.8, 105.5)
- removed the R11 at (155.8, 89.5)
- removed the R11 at (155.8, 73.5)
- removed the R11 at (155.8, 57.5)
- removed the R12 at (122.7, 120.5)
- removed the R12 at (122.7, 104.5)
- removed the R12 at (122.7, 88.5)
- removed the R12 at (122.7, 72.5)
- removed the R12 at (122.7, 56.5)
- removed the R13 at (167.6, 118.8)
- removed the R13 at (167.6, 102.8)
- removed the R13 at (167.6, 86.8)
- removed the R13 at (167.6, 70.8)
- removed the R13 at (167.6, 54.8)
- removed the R14 at (168.3, 120.7)
- removed the R14 at (168.3, 104.7)
- removed the R14 at (168.3, 88.7)
- removed the R14 at (168.3, 72.7)
- removed the R14 at (168.3, 56.7)
- removed the R15 at (169.7, 122.4)
- removed the R15 at (169.7, 106.4)
- removed the R15 at (169.7, 90.4)
- removed the R15 at (169.7, 74.4)
- removed the R15 at (169.7, 58.4)
- removed the R16 at (135.3, 118.5)
- removed the R16 at (135.3, 102.5)
- removed the R16 at (135.3, 86.5)
- removed the R16 at (135.3, 70.5)
- removed the R16 at (135.3, 54.5)
- removed the R17 at (155.5, 115.3)
- removed the R17 at (155.5, 99.3)
- removed the R17 at (155.5, 83.3)
- removed the R17 at (155.5, 67.3)
- removed the R17 at (155.5, 51.3)
- removed the R18 at (156.4, 123.7)
- removed the R18 at (156.4, 107.7)
- removed the R18 at (156.4, 91.7)
- removed the R18 at (156.4, 75.7)
- removed the R18 at (156.4, 59.7)
- removed the R2 at (157.6, 125.0)
- removed the R2 at (157.6, 109.0)
- removed the R2 at (157.6, 93.0)
- removed the R2 at (157.6, 77.0)
- removed the R2 at (157.6, 61.0)
- removed the R21 at (116.3, 118.8)
- removed the R21 at (116.3, 102.8)
- removed the R21 at (116.3, 86.8)
- removed the R21 at (116.3, 70.8)
- removed the R21 at (116.3, 54.8)
- removed the R22 at (165.4, 122.5)
- removed the R22 at (165.4, 106.5)
- removed the R22 at (165.4, 90.5)
- removed the R22 at (165.4, 74.5)
- removed the R22 at (165.4, 58.5)
- removed the R23 at (160.9, 123.9)
- removed the R23 at (160.9, 107.9)
- removed the R23 at (160.9, 91.9)
- removed the R23 at (160.9, 75.9)
- removed the R23 at (160.9, 59.9)
- removed the R24 at (118.6, 121.9)
- removed the R24 at (118.6, 105.9)
- removed the R24 at (118.6, 89.9)
- removed the R24 at (118.6, 73.9)
- removed the R24 at (118.6, 57.9)
- removed the R25 at (161.9, 118.0)
- removed the R25 at (161.9, 102.0)
- removed the R25 at (161.9, 86.0)
- removed the R25 at (161.9, 70.0)
- removed the R25 at (161.9, 54.0)
- removed the R26 at (119.0, 120.0)
- removed the R26 at (119.0, 104.0)
- removed the R26 at (119.0, 88.0)
- removed the R26 at (119.0, 72.0)
- removed the R26 at (119.0, 56.0)
- removed the R27 at (116.6, 120.9)
- removed the R27 at (116.6, 104.9)
- removed the R27 at (116.6, 88.9)
- removed the R27 at (116.6, 72.9)
- removed the R27 at (116.6, 56.9)
- removed the R28 at (166.3, 119.7)
- removed the R28 at (166.3, 103.7)
- removed the R28 at (166.3, 87.7)
- removed the R28 at (166.3, 71.7)
- removed the R28 at (166.3, 55.7)
- removed the R3 at (141.8, 118.5)
- removed the R3 at (141.8, 102.5)
- removed the R3 at (141.8, 86.5)
- removed the R3 at (141.8, 70.5)
- removed the R3 at (141.8, 54.5)
- removed the R31 at (147.8, 119.5)
- removed the R31 at (147.8, 103.5)
- removed the R31 at (147.8, 87.5)
- removed the R31 at (147.8, 71.5)
- removed the R31 at (147.8, 55.5)
- removed the R32 at (147.5, 115.2)
- removed the R32 at (147.5, 99.2)
- removed the R32 at (147.5, 83.2)
- removed the R32 at (147.5, 67.2)
- removed the R32 at (147.5, 51.2)
- removed the R33 at (145.8, 115.8)
- removed the R33 at (145.8, 99.8)
- removed the R33 at (145.8, 83.8)
- removed the R33 at (145.8, 67.8)
- removed the R33 at (145.8, 51.8)
- removed the R34 at (147.8, 118.0)
- removed the R34 at (147.8, 102.0)
- removed the R34 at (147.8, 86.0)
- removed the R34 at (147.8, 70.0)
- removed the R34 at (147.8, 54.0)
- removed the R35 at (145.8, 118.2)
- removed the R35 at (145.8, 102.2)
- removed the R35 at (145.8, 86.2)
- removed the R35 at (145.8, 70.2)
- removed the R35 at (145.8, 54.2)
- removed the R36 at (138.2, 125.8)
- removed the R36 at (138.2, 109.8)
- removed the R36 at (138.2, 93.8)
- removed the R36 at (138.2, 77.8)
- removed the R36 at (138.2, 61.8)
- removed the R37 at (147.8, 125.5)
- removed the R37 at (147.8, 109.5)
- removed the R37 at (147.8, 93.5)
- removed the R37 at (147.8, 77.5)
- removed the R37 at (147.8, 61.5)
- removed the R38 at (147.8, 124.2)
- removed the R38 at (147.8, 108.2)
- removed the R38 at (147.8, 92.2)
- removed the R38 at (147.8, 76.2)
- removed the R38 at (147.8, 60.2)
- removed the R4 at (141.8, 121.5)
- removed the R4 at (141.8, 105.5)
- removed the R4 at (141.8, 89.5)
- removed the R4 at (141.8, 73.5)
- removed the R4 at (141.8, 57.5)
- removed the R5 at (143.3, 119.0)
- removed the R5 at (143.3, 103.0)
- removed the R5 at (143.3, 87.0)
- removed the R5 at (143.3, 71.0)
- removed the R5 at (143.3, 55.0)
- removed the R6 at (145.0, 123.2)
- removed the R6 at (145.0, 107.2)
- removed the R6 at (145.0, 91.2)
- removed the R6 at (145.0, 75.2)
- removed the R6 at (145.0, 59.2)
- removed the R7 at (145.5, 125.0)
- removed the R7 at (145.5, 109.0)
- removed the R7 at (145.5, 93.0)
- removed the R7 at (145.5, 77.0)
- removed the R7 at (145.5, 61.0)
- removed the R8 at (143.0, 123.2)
- removed the R8 at (143.0, 107.2)
- removed the R8 at (143.0, 91.2)
- removed the R8 at (143.0, 75.2)
- removed the R8 at (143.0, 59.2)
- removed the R9 at (135.8, 120.0)
- removed the R9 at (135.8, 104.0)
- removed the R9 at (135.8, 88.0)
- removed the R9 at (135.8, 72.0)
- removed the R9 at (135.8, 56.0)
- removed the REF** at (104.5, 120.5)
- removed the REF** at (180.5, 56.5)
- removed the REF** at (180.5, 40.5)
- removed the REF** at (104.5, 40.5)
- removed the REF** at (104.5, 104.5)
- removed the REF** at (104.5, 88.5)
- removed the REF** at (104.5, 72.5)
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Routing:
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- added copper zone on F.Cu, net Net-(D11-Pad1)
- added copper zone on F.Cu, net Net-(D12-Pad1)
- added copper zone on F.Cu, net Net-(D15-Pad1)
- added copper zone on F.Cu, net Net-(D16-Pad1)
- added copper zone on F.Cu, net Net-(R10-Pad1)
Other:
- outline, holes or cut-outs redrawn
- rule pad_to_mask_clearance: 0.05 -> 0
- board text added: "<- FWD"
- board text added: "K3057RA"
- board text added: "K3057RA Rev.3 2022.01"
- board text added: "REV ->"
- board text added: "Rev.3 2022.01"
- board text removed: "K3057RA Rev.2 2021.05"
- board text removed: "Rev.2 2021.05"
